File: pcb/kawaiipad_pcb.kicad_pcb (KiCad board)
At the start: 2 copper layers, 65 x 85 mm, 28 parts, among them SW1 SW_Push_45deg, SW2 SW_Push_45deg, SW3 SW_Push_45deg, SW4 SW_Push_45deg, SW5 SW_Push_45deg, SW6 SW_Push_45deg, SW7 SW_Push_45deg, SW8 SW_Push_45deg, SW9 SW_Push_45deg, U1 XIAO-RP2040-DIP

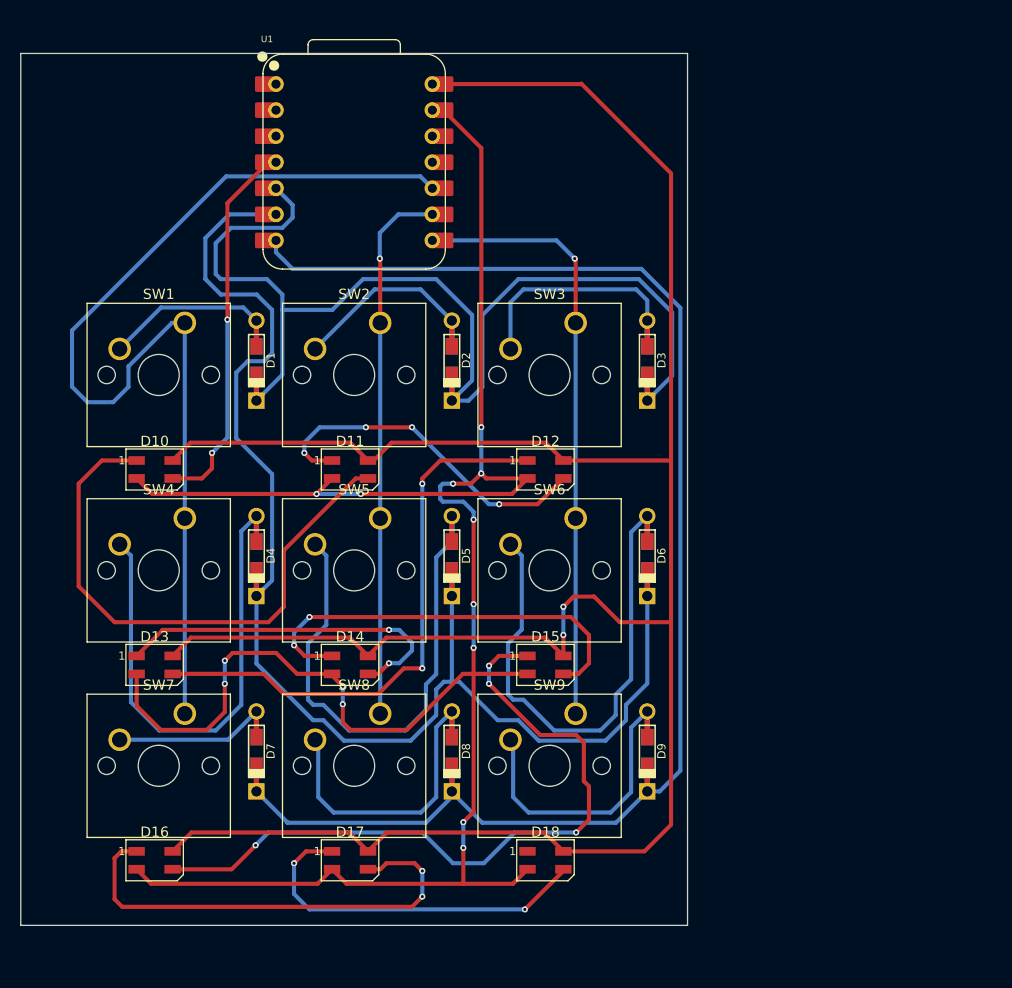
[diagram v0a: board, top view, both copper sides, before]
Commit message: rearrange led on pcb
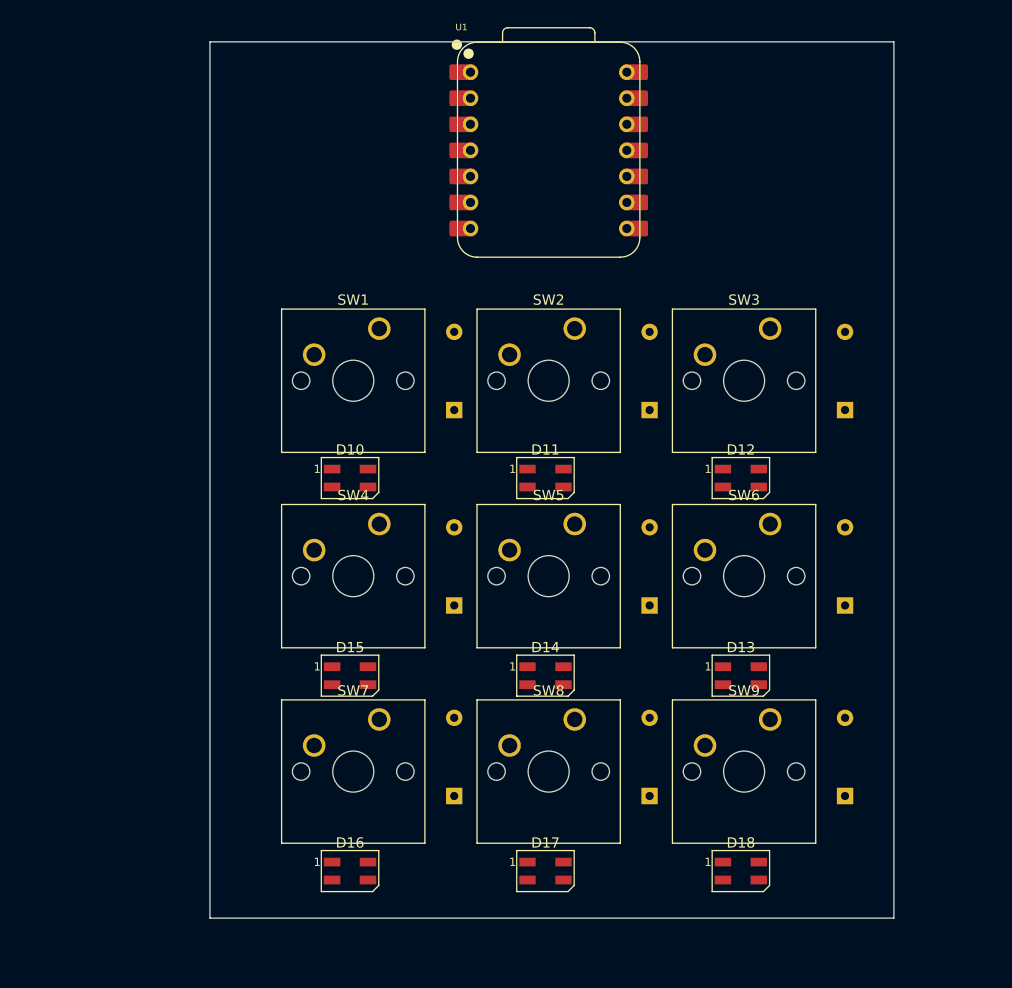
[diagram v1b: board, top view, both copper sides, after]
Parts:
- D1, D2, D3, D4, D5, D6, D7, D8, D9: footprint DiodeLibrary:Diode-Hybrid-Dual -> Diode_THT:D_DO-35_SOD27_P7.62mm_Horizontal
- moved D13 57.2 mm to (166.1, 109.7)
- moved D4 19.9 mm to (138.1, 102.9), turned to 90 degrees
- moved D1 19.9 mm to (138.1, 83.8), turned to 90 degrees
- moved D5 19.9 mm to (157.2, 102.9), turned to 90 degrees
- moved D6 19.9 mm to (176.2, 102.9), turned to 90 degrees
- moved D2 19.9 mm to (157.2, 83.8), turned to 90 degrees
- moved D3 19.9 mm to (176.2, 83.8), turned to 90 degrees
- moved D7 19.8 mm to (138.1, 121.4), turned to 90 degrees
- moved D8 19.8 mm to (157.2, 121.4), turned to 90 degrees
- moved D9 19.8 mm to (176.2, 121.4), turned to 90 degrees
- moved D18 19.1 mm to (166.1, 128.8)
- moved D14 19.1 mm to (147.0, 109.7)
- moved D15 19.1 mm to (128.0, 109.7)
- moved D16 19.1 mm to (128.0, 128.8)
- moved D17 19.1 mm to (147.0, 128.8)
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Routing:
- net +5V: track 251.6 -> 0.00 mm, vias 2 -> 0
- net GND: track 226.6 -> 0.00 mm, vias 14 -> 0
- net Row 2: track 135.5 -> 0.00 mm
- net Row 1: track 126.0 -> 0.00 mm
- net Row 0: track 107.0 -> 0.00 mm
- net Column 0: track 101.4 -> 0.00 mm
- net Net-(D15-DOUT): track 70.3 -> 0.00 mm, vias 4 -> 0
- net Column 2: track 59.0 -> 0.00 mm, vias 1 -> 0
- net Net-(D12-DOUT): track 55.7 -> 0.00 mm, vias 2 -> 0
- net Net-(D10-DOUT): track 55.3 -> 0.00 mm
- net Column 1: track 52.8 -> 0.00 mm, vias 1 -> 0
- net Net-(D6-A): track 48.9 -> 0.00 mm
- net Net-(D4-A): track 47.8 -> 0.00 mm
- net Net-(D5-A): track 47.4 -> 0.00 mm
- net Net-(D16-DOUT): track 45.5 -> 0.00 mm, vias 2 -> 0
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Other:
- board size 65 x 85 mm -> 66.7 x 85.4 mm

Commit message: add leds, edge cuts, properly measured
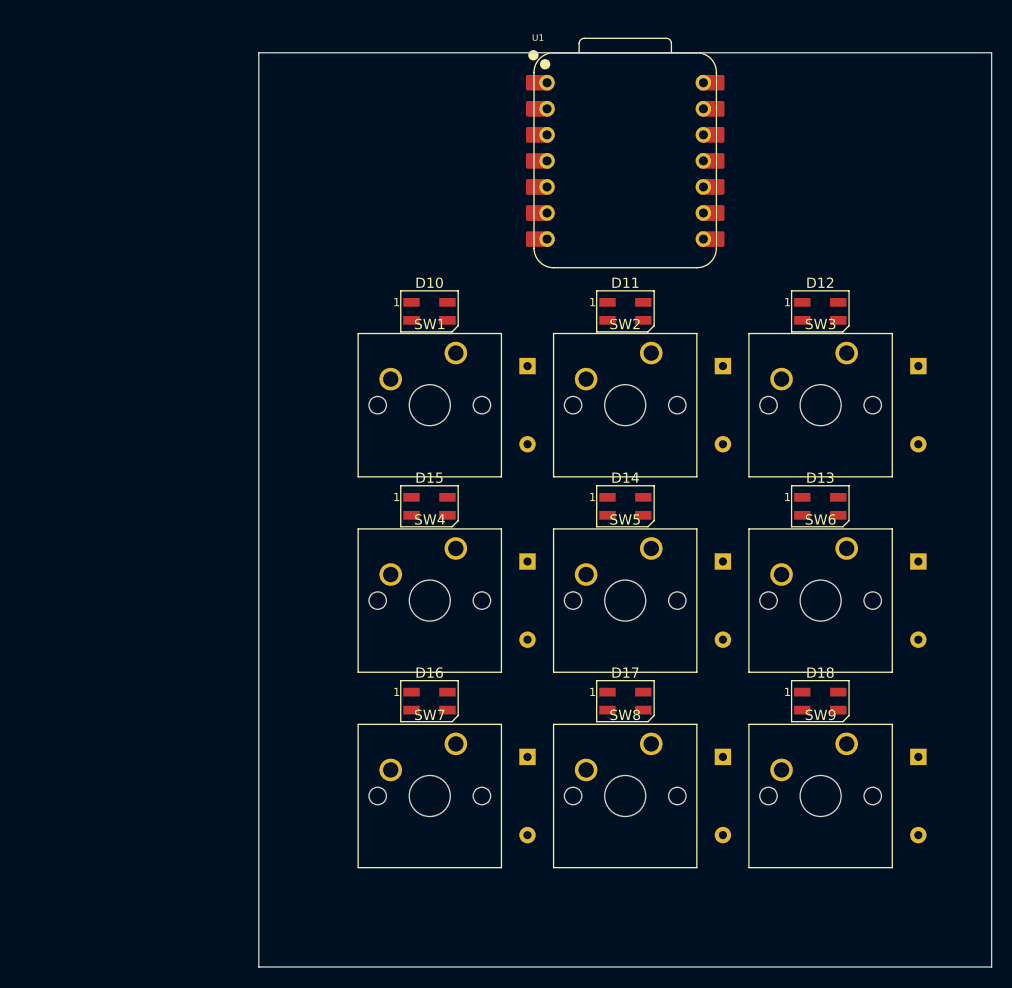
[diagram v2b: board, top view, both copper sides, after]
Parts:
- moved D17 18.3 mm to (154.8, 112.2)
- moved D18 18.3 mm to (173.8, 112.2)
- moved D16 18.3 mm to (135.7, 112.2)
- moved D14 18.3 mm to (154.8, 93.2)
- moved D13 18.2 mm to (173.8, 93.2)
- moved D15 18.2 mm to (135.7, 93.2)
- moved D11 18.0 mm to (154.8, 74.2)
- moved D12 18.0 mm to (173.8, 74.2)
- moved D10 18.0 mm to (135.7, 74.2)
- moved D5 8.33 mm to (164.3, 98.6), turned to -90 degrees
- moved D2 8.33 mm to (164.3, 79.5), turned to -90 degrees
- moved D4 8.33 mm to (145.3, 98.6), turned to -90 degrees
- moved D6 8.33 mm to (183.4, 98.6), turned to -90 degrees
- moved D1 8.33 mm to (145.3, 79.5), turned to -90 degrees
- moved D3 8.33 mm to (183.4, 79.5), turned to -90 degrees
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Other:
- board size 66.7 x 85.4 mm -> 71.4 x 89.1 mm

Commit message: redesign pcb w/o gnd
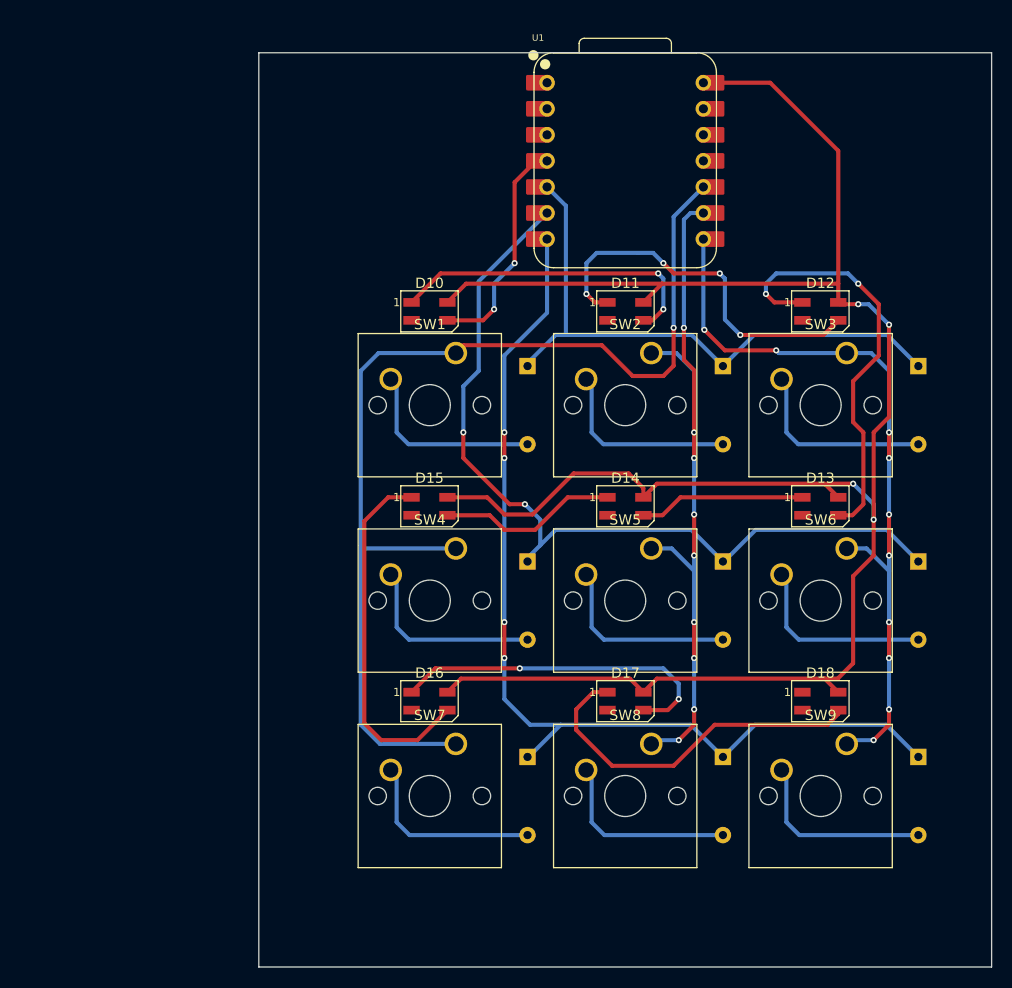
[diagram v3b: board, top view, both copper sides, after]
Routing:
- net +5V: track 0.00 -> 206.2 mm, vias 0 -> 4
- net Column 0: track 0.00 -> 105.8 mm, vias 0 -> 1
- net Row 2: track 0.00 -> 96.4 mm, vias 0 -> 4
- net Row 1: track 0.00 -> 83.2 mm, vias 0 -> 2
- net Column 2: track 0.00 -> 73.0 mm, vias 0 -> 10
- net Column 1: track 0.00 -> 72.8 mm, vias 0 -> 9
- net Row 0: track 0.00 -> 58.5 mm
- net Net-(D12-DOUT): track 0.00 -> 41.4 mm, vias 0 -> 2
- net Net-(D11-DOUT): track 0.00 -> 36.6 mm, vias 0 -> 4
- net Net-(D15-DOUT): track 0.00 -> 35.3 mm
- net Net-(D17-DOUT): track 0.00 -> 35.2 mm
- net Net-(D16-DOUT): track 0.00 -> 33.0 mm, vias 0 -> 2
- net Net-(D10-DOUT): track 0.00 -> 31.4 mm, vias 0 -> 2
- net LED: track 0.00 -> 22.2 mm, vias 0 -> 2
- net Net-(D3-A): track 0.00 -> 18.7 mm
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
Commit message: add groundpour
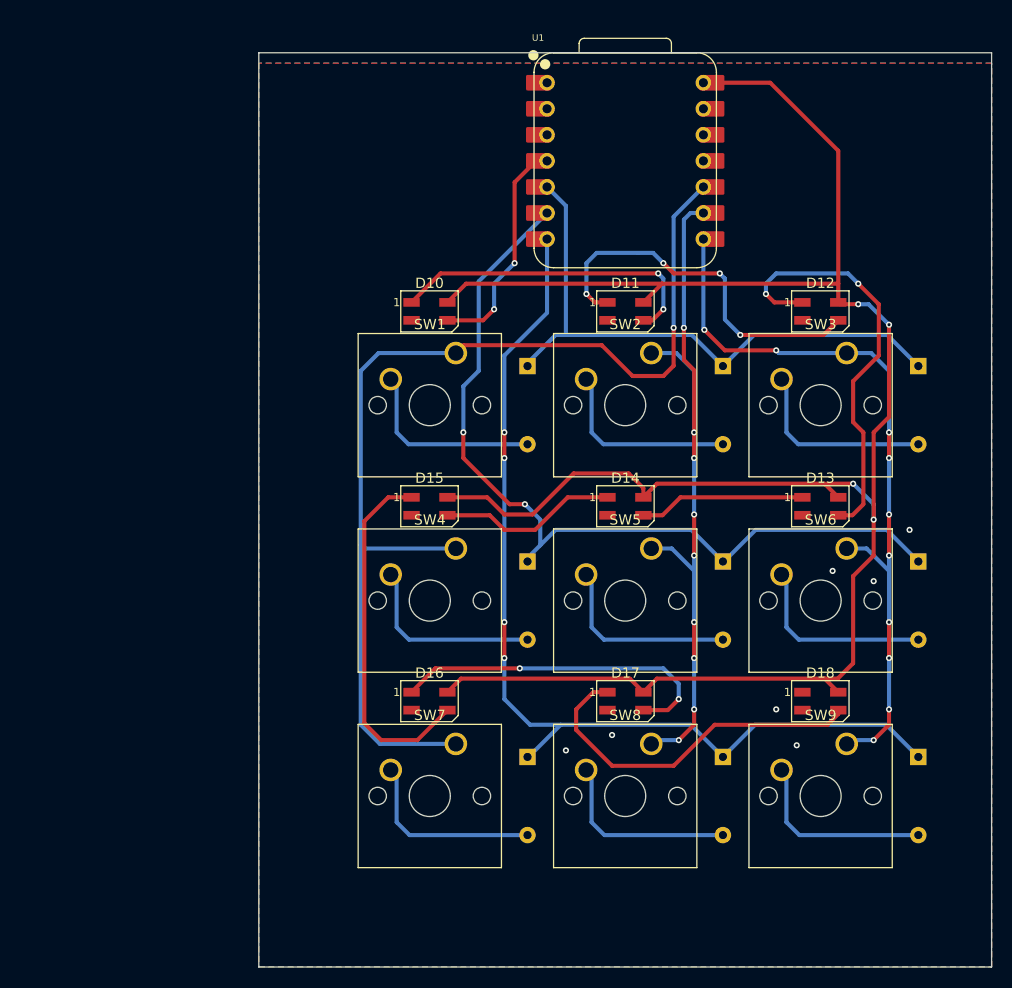
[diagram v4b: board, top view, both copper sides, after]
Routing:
- net GND: vias 0 -> 7
- added copper zone on B.Cu, net GND
- added copper zone on F.Cu, net GND
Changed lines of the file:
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@@
 		(net 13)
+	)
+	(via
+		(at 175 99.5)
+		(size 0.6)
+		(drill 0.3)
+		(layers "F.Cu" "B.Cu")
+		(free yes)
+		(net 14)
+	)
+	(via
+		(at 182.5 95.5)
+		(size 0.6)
+		(drill 0.3)
+		(layers "F.Cu" "B.Cu")
+		(free yes)
+		(net 14)
+	)
+	(via
+		(at 171.5 116.5)
+		(size 0.6)
+		(drill 0.3)
+		(layers "F.Cu" "B.Cu")
+		(free yes)
+		(net 14)
+	)
+	(via
+		(at 153.5 115.5)
+		(size 0.6)
+		(drill 0.3)
+		(layers "F.Cu" "B.Cu")
+		(free yes)
+		(net 14)
+	)
+	(via
+		(at 179 100.5)
+		(size 0.6)
+		(drill 0.3)
+		(layers "F.Cu" "B.Cu")
+		(free yes)
+		(net 14)
+	)
+	(via
+		(at 169.5 113)
+		(size 0.6)
+		(drill 0.3)
+		(layers "F.Cu" "B.Cu")
+		(free yes)
+		(net 14)
+	)
+	(via
+		(at 149 117)
+		(size 0.6)
+		(drill 0.3)
+		(layers "F.Cu" "B.Cu")
+		(free yes)
+		(net 14)
 	)
 	(segment
@@
 		(net 36)
 	)
+	(zone
+		(net 14)
+		(net_name "GND")
+		(layers "F&B.Cu")
+		(hatch edge 0.5)
+		(connect_pads
+			(clearance 0.5)
+		)
+		(min_thickness 0.25)
+		(filled_areas_thickness no)
+		(fill yes
+			(thermal_gap 0.5)
+			(thermal_bridge_width 0.5)
+		)
+		(polygon
+			(pts
+				(xy 119.0625 138.1125) (xy 190.5 138.1125) (xy 190.5 50.00625) (xy 119.0625 50.00625)
+			)
+		)
+	)
 )

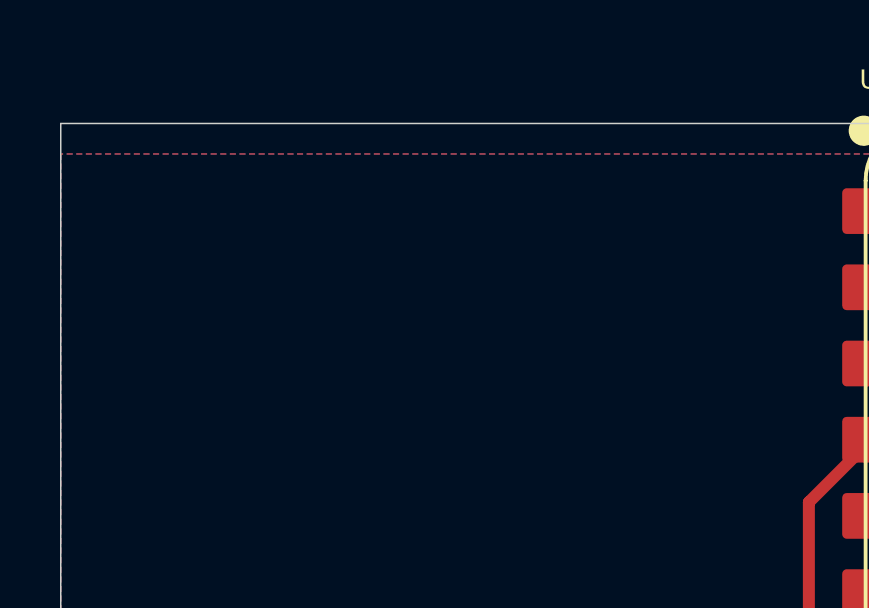
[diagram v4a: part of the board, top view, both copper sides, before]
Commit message: add silkscreen art
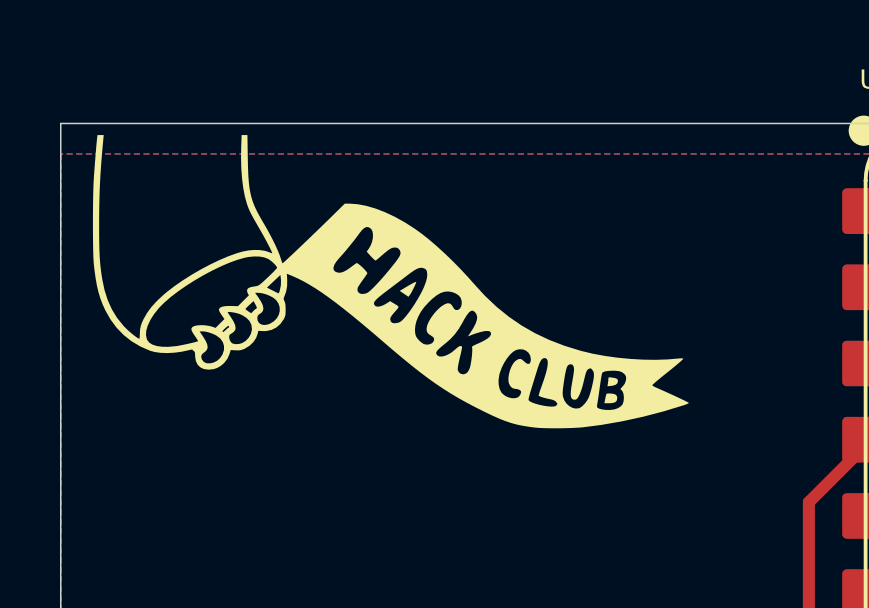
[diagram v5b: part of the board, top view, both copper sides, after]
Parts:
- added G***: LOGO, LOGO, F.Cu at (130.0, 55.0)
- added G***: LOGO, LOGO, B.Cu at (157.0, 97.5)

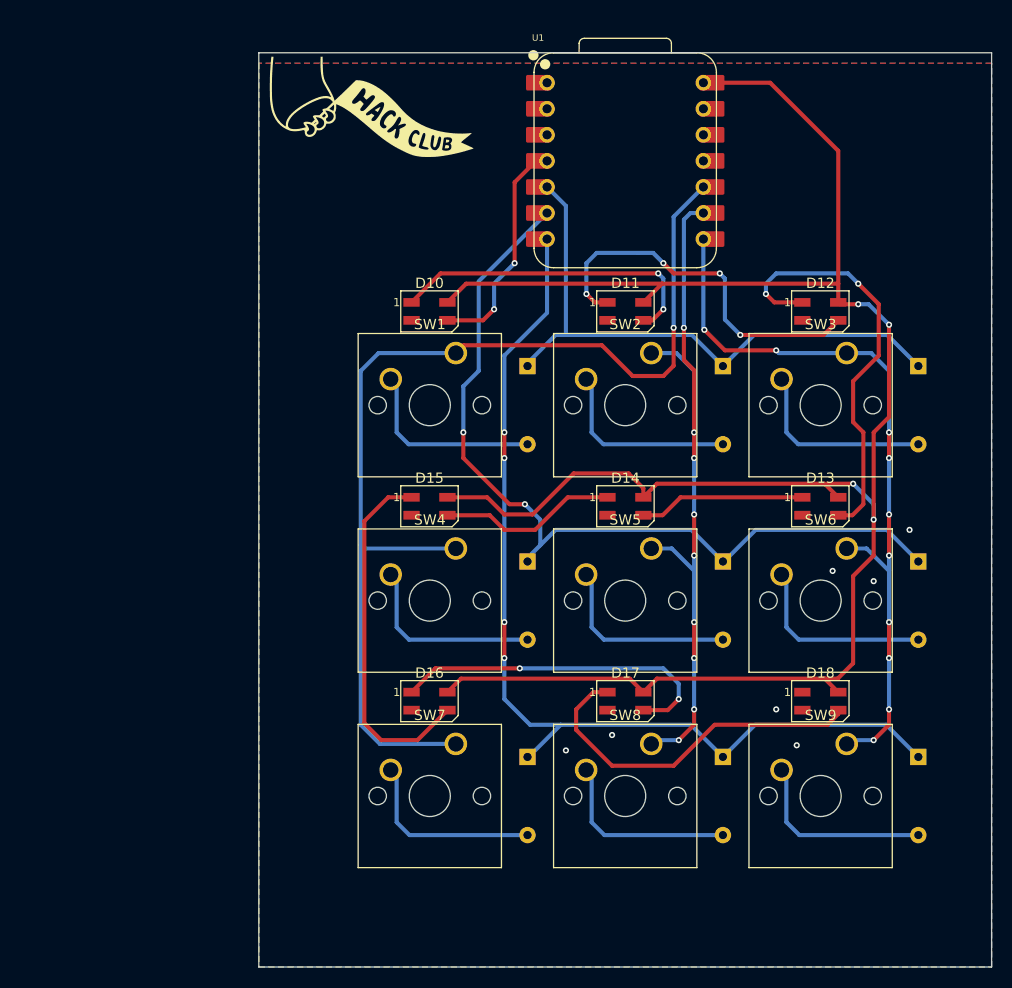
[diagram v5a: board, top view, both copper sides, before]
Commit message: update pcb text + add ssart
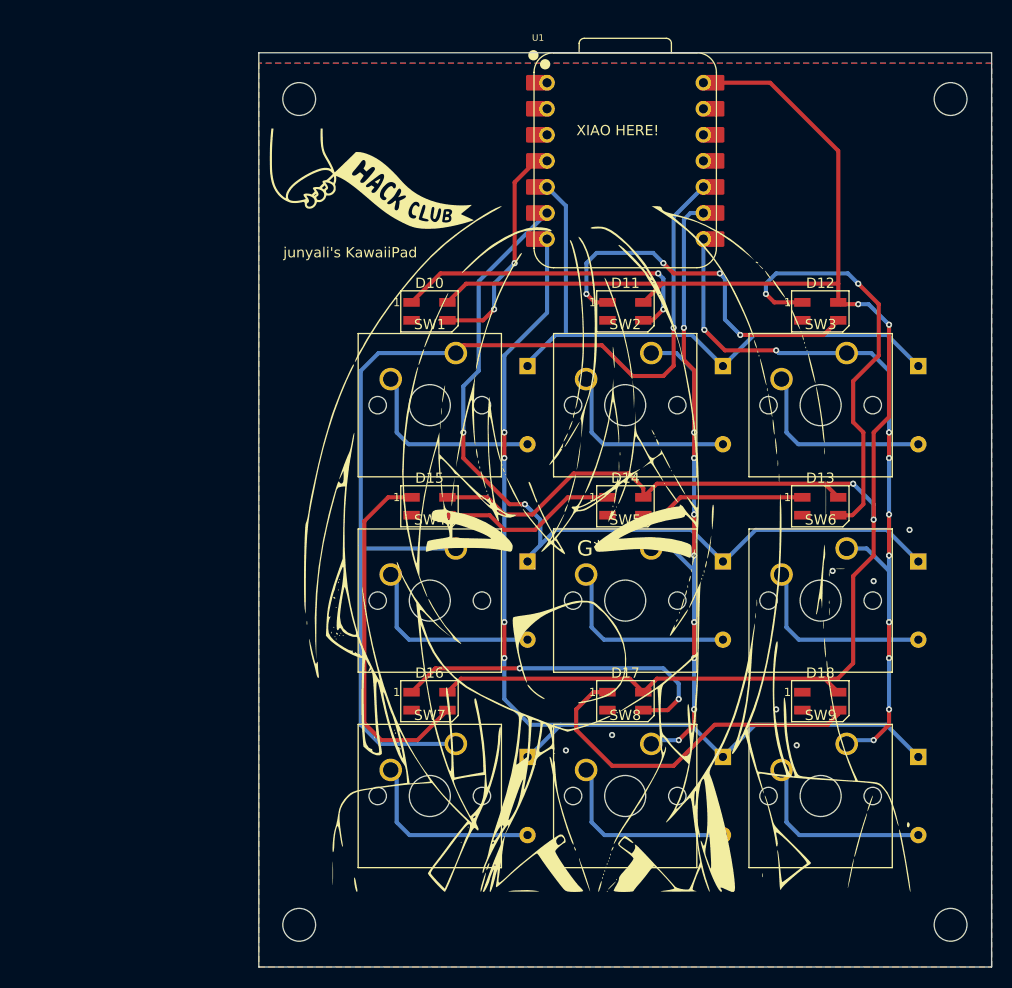
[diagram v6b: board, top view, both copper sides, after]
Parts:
- added G***: LOGO, LOGO, B.Cu at (154.8, 81.0)
- added REF**: M3 Screw, MountingHole:MountingHole_3.2mm_M3, F.Cu at (186.5, 134.0)
- added REF**: M3 Screw, MountingHole:MountingHole_3.2mm_M3, F.Cu at (186.5, 53.5)
- added REF**: M3 Screw, MountingHole:MountingHole_3.2mm_M3, F.Cu at (123.0, 134.0)
- added REF**: M3 Screw, MountingHole:MountingHole_3.2mm_M3, F.Cu at (123.0, 53.5)
- G***: moved to F.Cu
- moved G*** 7.00 mm to (130.0, 62.0)
- moved G*** 4.60 mm to (152.4, 97.3), turned to 0 degrees
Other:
- board text added: "Reimu :3"
- board text added: "XIAO HERE!"
- board text added: "junyali's KawaiiPad"
